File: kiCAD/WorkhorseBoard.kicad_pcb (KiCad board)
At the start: 4 copper layers, 205 x 97 mm, 385 parts, among them J1 USB_B_Mini, J10 MAIN_POWER, J11 BED_POWER, J12 H0, J13 F0, J14 5V_EXT, J15 F1, J16 F4, J17 H1, J19 F2, J2 Micro_SD_Card, J20 F5, J21 H2, J22 F3, J23 HB, J24 Conn_01x02, J25 Conn_01x02, J26 Conn_01x02, J27 Conn_01x02, J28 Conn_01x03, J29 Conn_01x03, J3 Conn_01x06, J30 Conn_01x03, J31 Conn_01x03, J32 Conn_01x03, J33 Conn_01x03, J4 X, J5 E0, J6 Y, J7 E1, J8 Z, J9 E2, Q1 Q_NMOS_GSD, Q10 Q_NMOS_GDS, Q2 Q_NMOS_GDS, Q3 Q_NMOS_GSD, Q4 Q_NMOS_GSD, Q5 Q_NMOS_GDS, Q6 Q_NMOS_GSD, Q7 Q_NMOS_GSD, Q8 Q_NMOS_GDS, Q9 Q_NMOS_GSD, SW1 SW_Push, U1 24C02, U10 TPS54531, U11 TPS54531, U12 AP7361C-33E-13, U13 74HCT365, U14 74HCT365, U2 USBLC6-2SC6, U3 STM32F446VETx, U4 TMC2209, U5 TMC2209, U6 TMC2209, U7 TMC2209, U8 TMC2209, U9 TMC2209, Y1 X322512MSB4SI

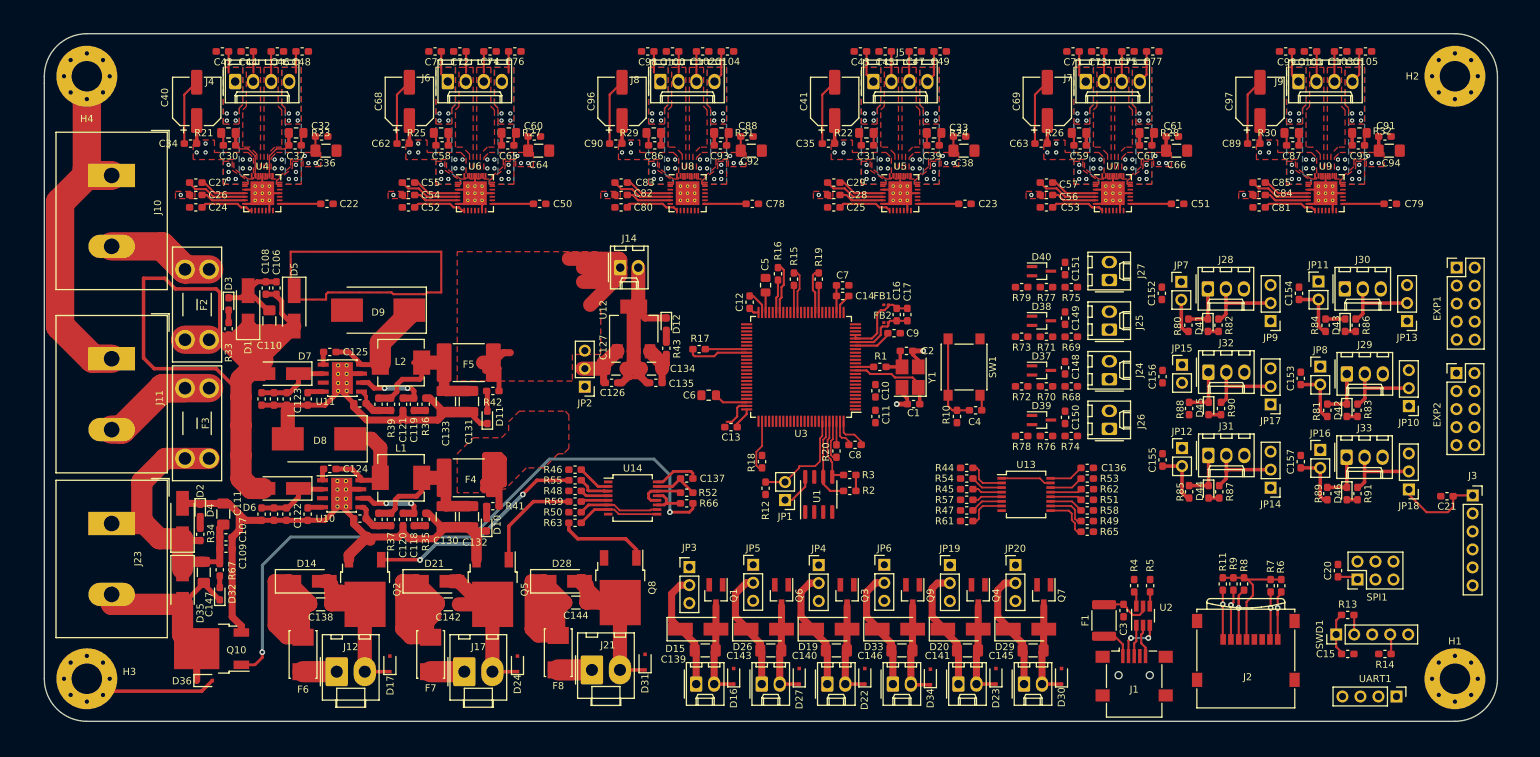
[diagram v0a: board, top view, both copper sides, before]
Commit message: refined some of the fills, started routing.
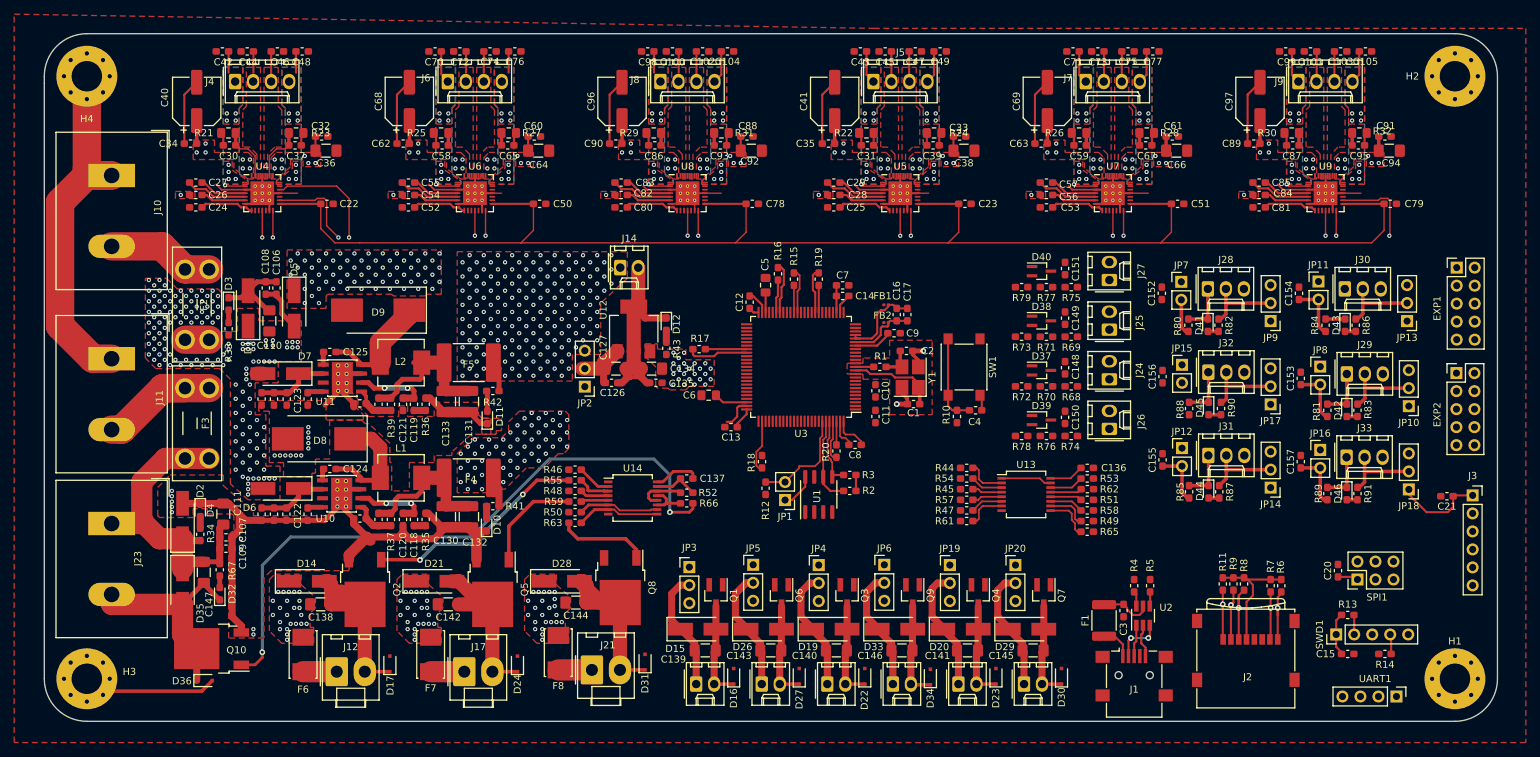
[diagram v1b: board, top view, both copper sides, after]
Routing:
- net +24V: track 248.9 -> 11.4 mm, vias 0 -> 215
- net +3V3: track 93.5 -> 269.1 mm, vias 0 -> 23
- net VM: track 87.4 -> 35.3 mm, vias 90 -> 157
- net +5V: track 62.3 -> 31.3 mm, vias 0 -> 172
- net GND: track 448.6 -> 469.7 mm, vias 2 -> 22
- net X_DIR: track 0.00 -> 16.2 mm, vias 0 -> 1
- net +12V: track 20.2 -> 4.99 mm, vias 0 -> 55
- net X_STEP: track 0.00 -> 12.8 mm, vias 0 -> 1
- net E2_STEP: track 0.00 -> 11.9 mm, vias 0 -> 1
- net X_RX: track 6.31 -> 10.1 mm, vias 0 -> 1
- net X_DIAG: track 0.00 -> 3.80 mm, vias 0 -> 1
- net Z_RX: track 8.64 -> 12.2 mm, vias 0 -> 1
- net Z_DIAG: track 0.00 -> 3.55 mm, vias 0 -> 1
- net Y_RX: track 7.20 -> 10.7 mm, vias 0 -> 1
- net Y_DIAG: track 0.00 -> 3.55 mm, vias 0 -> 1
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- added copper zone on F.Cu, net +3V3
- added copper zone on F.Cu, net GND
- added copper zone on In2.Cu, net GND

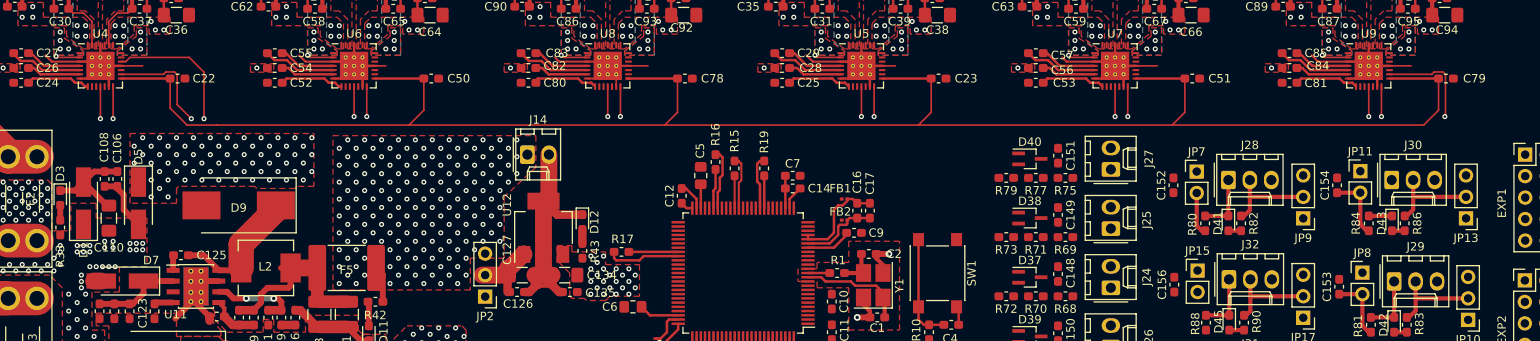
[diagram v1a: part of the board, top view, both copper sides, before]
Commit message: slight change to TMC layout.
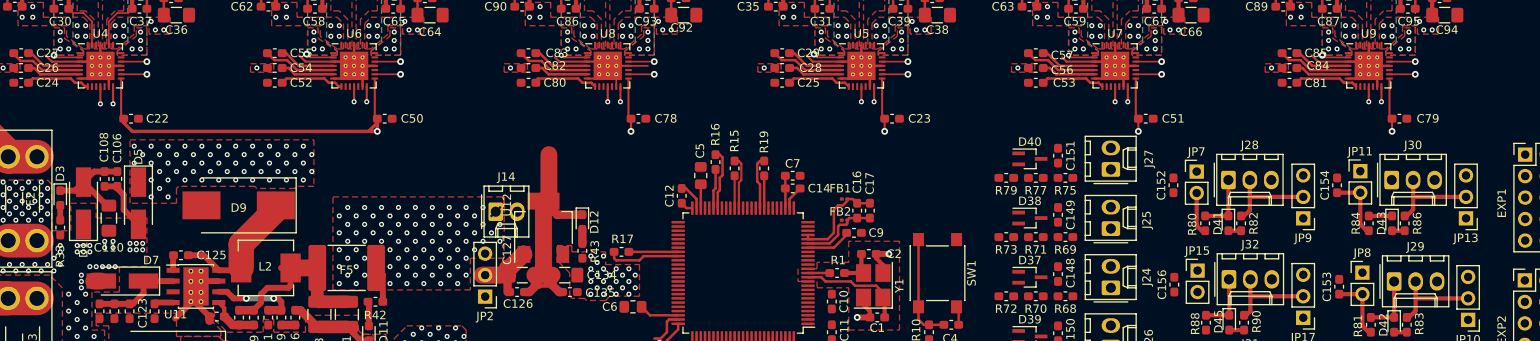
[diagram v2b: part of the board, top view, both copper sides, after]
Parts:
- moved J14 7.72 mm to (103.5, 68.8)
- moved C22 7.27 mm to (60.4, 57.8)
- moved C23 7.27 mm to (150.4, 57.8)
- moved C50 7.27 mm to (90.4, 57.8)
- moved C51 7.27 mm to (180.4, 57.8)
- moved C78 7.27 mm to (120.4, 57.8)
- moved C79 7.27 mm to (210.4, 57.8)
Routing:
- net +3V3: track 269.1 -> 120.2 mm, vias 23 -> 28
- net X_DIR: track 16.2 -> 3.05 mm
- net GND: track 469.7 -> 459.2 mm
- net X_STEP: track 12.8 -> 3.05 mm
- net E2_STEP: track 11.9 -> 3.05 mm
- net E2_DIR: track 0.00 -> 3.05 mm, vias 0 -> 1
- net E1_STEP: track 0.00 -> 3.05 mm, vias 0 -> 1
- net E1_DIR: track 0.00 -> 3.05 mm, vias 0 -> 1
- net E0_STEP: track 0.00 -> 3.05 mm, vias 0 -> 1
- net E0_DIR: track 0.00 -> 3.05 mm, vias 0 -> 1
- net Z_STEP: track 0.00 -> 3.05 mm, vias 0 -> 1
- net Z_DIR: track 0.00 -> 3.05 mm, vias 0 -> 1
- net Y_STEP: track 0.00 -> 3.05 mm, vias 0 -> 1
- net Y_DIR: track 0.00 -> 3.05 mm, vias 0 -> 1
- net Z_RX: track 12.2 -> 10.4 mm
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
